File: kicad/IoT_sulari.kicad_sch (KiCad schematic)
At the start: 29 parts, among them J1 73412-0110, J2 73412-0110, J3 20021121-00010C4LF, J4 20021121-00010C4LF, J6 20021121-00010C4LF, SW1 SW_SPST, SW2 TL3301DF160QG, SW3 TL3301DF160QG, SW4 TL3301DF160QG, SW5 TL3301DF160QG, U2 NRF9160-SICA-B1A-R

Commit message: moro
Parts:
- added H1, H2, H3, H4: MountingHole_Pad, MountingHole:MountingHole_3.2mm_M3_Pad_Via, symbol Mechanical:MountingHole_Pad
- U2: value NRF9160-SICA-B1A-R -> NRF9160
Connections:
- net GND: now also J3.3, J3.5, H1.1, H2.1, H3.1, H4.1
- net SWDCLK: now also J3.4; no longer J3.5, J3.6
- net SWDIO: now also J3.2; no longer J3.4, J3.7
- net NRESET: now reaches C10.1, R2.1, U2.32 (NRESET)
- net NRESET: now also J3.10
- no-connect marks 13 -> 15
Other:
- moved on the sheet: D1, D2, R3, R4

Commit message: added board outline and inner copper layers, layout finalization
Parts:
- added R5, R6, R7, R8: 10k, Resistor_SMD:R_0603_1608Metric_Pad0.98x0.95mm_HandSolder, symbol Device:R
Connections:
- net GND: now also R5.1, R6.1, R7.1, R8.1; no longer SW2.3, SW2.4, SW3.3, SW3.4, SW4.3, SW4.4, SW5.3, SW5.4
- new net: R8.2, SW5.3, SW5.4
- new net: R6.2, SW3.3, SW3.4
- new net: R7.2, SW4.3, SW4.4
- new net: R5.2, SW2.3, SW2.4
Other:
- removed sheet sensorboard

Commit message: routing
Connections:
- net BUSY: now also U2.26 (P0-16/AIN3); no longer U2.29 (P0-18/AIN5)
- net CS: now also U2.28 (P0-17/AIN4); no longer U2.25 (P0-15/AIN2)
- net DC: now also U2.25 (P0-15/AIN2); no longer U2.26 (P0-16/AIN3)
- net RST: now also U2.29 (P0-18/AIN5); no longer U2.28 (P0-17/AIN4)
- net SCL: now also U2.86 (P0-28); no longer U2.84 (P0-27)
- net SDA: now also U2.84 (P0-27); no longer U2.83 (P0-26)
- net TMP_ALERT: now also U2.83 (P0-26); no longer U2.86 (P0-28)
- net +3.3V: no longer names the net of C1.1, C2.1, C3.1, FB1.2
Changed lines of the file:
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@@
-    (effects (font (size 1.27 1.27)) (justify left bottom))
-  )
-  (label "+3.3V" (at 101.6 24.13 0) (fields_autoplaced)
     (effects (font (size 1.27 1.27)) (justify left bottom))
   )
@@
     )
   )
-  (global_label "TMP_ALERT" (shape input) (at 222.25 111.76 0) (fields_autoplaced)
+  (global_label "TMP_ALERT" (shape input) (at 222.25 106.68 0) (fields_autoplaced)
     (effects (font (size 1.27 1.27)) (justify left))
-    (property "Intersheetrefs" "${INTERSHEET_REFS}" (at 235.3157 111.76 0)
+    (property "Intersheetrefs" "${INTERSHEET_REFS}" (at 235.3157 106.68 0)
       (effects (font (size 1.27 1.27)) (justify left) hide)
     )
   )
-  (global_label "BUSY" (shape input) (at 152.4 119.38 180) (fields_autoplaced)
-    (effects (font (size 1.27 1.27)) (justify right))
-    (property "Intersheetrefs" "${INTERSHEET_REFS}" (at 144.5956 119.38 0)
+  (global_label "BUSY" (shape input) (at 152.4 114.3 180) (fields_autoplaced)
+    (effects (font (size 1.27 1.27)) (justify right))
+    (property "Intersheetrefs" "${INTERSHEET_REFS}" (at 144.5956 114.3 0)
       (effects (font (size 1.27 1.27)) (justify right) hide)
     )
@@
     )
   )
-  (global_label "RST" (shape input) (at 152.4 116.84 180) (fields_autoplaced)
-    (effects (font (size 1.27 1.27)) (justify right))
-    (property "Intersheetrefs" "${INTERSHEET_REFS}" (at 146.0471 116.84 0)
+  (global_label "RST" (shape input) (at 152.4 119.38 180) (fields_autoplaced)
+    (effects (font (size 1.27 1.27)) (justify right))
+    (property "Intersheetrefs" "${INTERSHEET_REFS}" (at 146.0471 119.38 0)
       (effects (font (size 1.27 1.27)) (justify right) hide)
     )
@@
     )
   )
-  (global_label "CS" (shape input) (at 152.4 111.76 180) (fields_autoplaced)
-    (effects (font (size 1.27 1.27)) (justify right))
-    (property "Intersheetrefs" "${INTERSHEET_REFS}" (at 147.0147 111.76 0)
+  (global_label "CS" (shape input) (at 152.4 116.84 180) (fields_autoplaced)
+    (effects (font (size 1.27 1.27)) (justify right))
+    (property "Intersheetrefs" "${INTERSHEET_REFS}" (at 147.0147 116.84 0)
       (effects (font (size 1.27 1.27)) (justify right) hide)
     )
@@
     )
   )
-  (global_label "SCL" (shape input) (at 222.25 109.22 0) (fields_autoplaced)
+  (global_label "SCL" (shape input) (at 222.25 111.76 0) (fields_autoplaced)
     (effects (font (size 1.27 1.27)) (justify left))
-    (property "Intersheetrefs" "${INTERSHEET_REFS}" (at 228.6634 109.22 0)
+    (property "Intersheetrefs" "${INTERSHEET_REFS}" (at 228.6634 111.76 0)
       (effects (font (size 1.27 1.27)) (justify left) hide)
     )
@@
     )
   )
-  (global_label "DC" (shape input) (at 152.4 114.3 180) (fields_autoplaced)
-    (effects (font (size 1.27 1.27)) (justify right))
-    (property "Intersheetrefs" "${INTERSHEET_REFS}" (at 146.9542 114.3 0)
+  (global_label "DC" (shape input) (at 152.4 111.76 180) (fields_autoplaced)
+    (effects (font (size 1.27 1.27)) (justify right))
+    (property "Intersheetrefs" "${INTERSHEET_REFS}" (at 146.9542 111.76 0)
       (effects (font (size 1.27 1.27)) (justify right) hide)
     )
@@
     )
   )
-  (global_label "SDA" (shape input) (at 222.25 106.68 0) (fields_autoplaced)
+  (global_label "SDA" (shape input) (at 222.25 109.22 0) (fields_autoplaced)
     (effects (font (size 1.27 1.27)) (justify left))
-    (property "Intersheetrefs" "${INTERSHEET_REFS}" (at 228.7239 106.68 0)
+    (property "Intersheetrefs" "${INTERSHEET_REFS}" (at 228.7239 109.22 0)
       (effects (font (size 1.27 1.27)) (justify left) hide)
     )
@@
   (symbol (lib_name "+3.3V_2") (lib_id "power:+3.3V") (at 86.36 21.59 0) (unit 1)
     (in_bom yes) (on_board yes) (dnp no) (fields_autoplaced)
-    (property "Reference" "#PWR011" (at 86.36 25.4 0)
+    (property "Reference" "#PWR0106" (at 86.36 25.4 0)
       (effects (font (size 1.27 1.27)) hide)
     )
@@
       (project "IoT_sulari"
         (path "/184b47ed-2c2b-4c02-be35-d18f4f4e5685"
-          (reference "#PWR011") (unit 1)
+          (reference "#PWR0106") (unit 1)
         )
       )
@@
   (symbol (lib_name "+3.3V_1") (lib_id "power:+3.3V") (at 123.19 31.75 0) (unit 1)
     (in_bom yes) (on_board yes) (dnp no) (fields_autoplaced)
-    (property "Reference" "#PWR012" (at 123.19 35.56 0)
+    (property "Reference" "#PWR0104" (at 123.19 35.56 0)
       (effects (font (size 1.27 1.27)) hide)
     )
@@
       (project "IoT_sulari"
         (path "/184b47ed-2c2b-4c02-be35-d18f4f4e5685"
-          (reference "#PWR012") (unit 1)
+          (reference "#PWR0104") (unit 1)
         )
       )
@@
   (symbol (lib_name "+3.3V_3") (lib_id "power:+3.3V") (at 118.11 48.26 0) (unit 1)
     (in_bom yes) (on_board yes) (dnp no) (fields_autoplaced)
-    (property "Reference" "#PWR025" (at 118.11 52.07 0)
+    (property "Reference" "#PWR0105" (at 118.11 52.07 0)
       (effects (font (size 1.27 1.27)) hide)
     )
@@
       (project "IoT_sulari"
         (path "/184b47ed-2c2b-4c02-be35-d18f4f4e5685"
-          (reference "#PWR025") (unit 1)
-        )
-      )
+          (reference "#PWR0105") (unit 1)
+        )
+      )

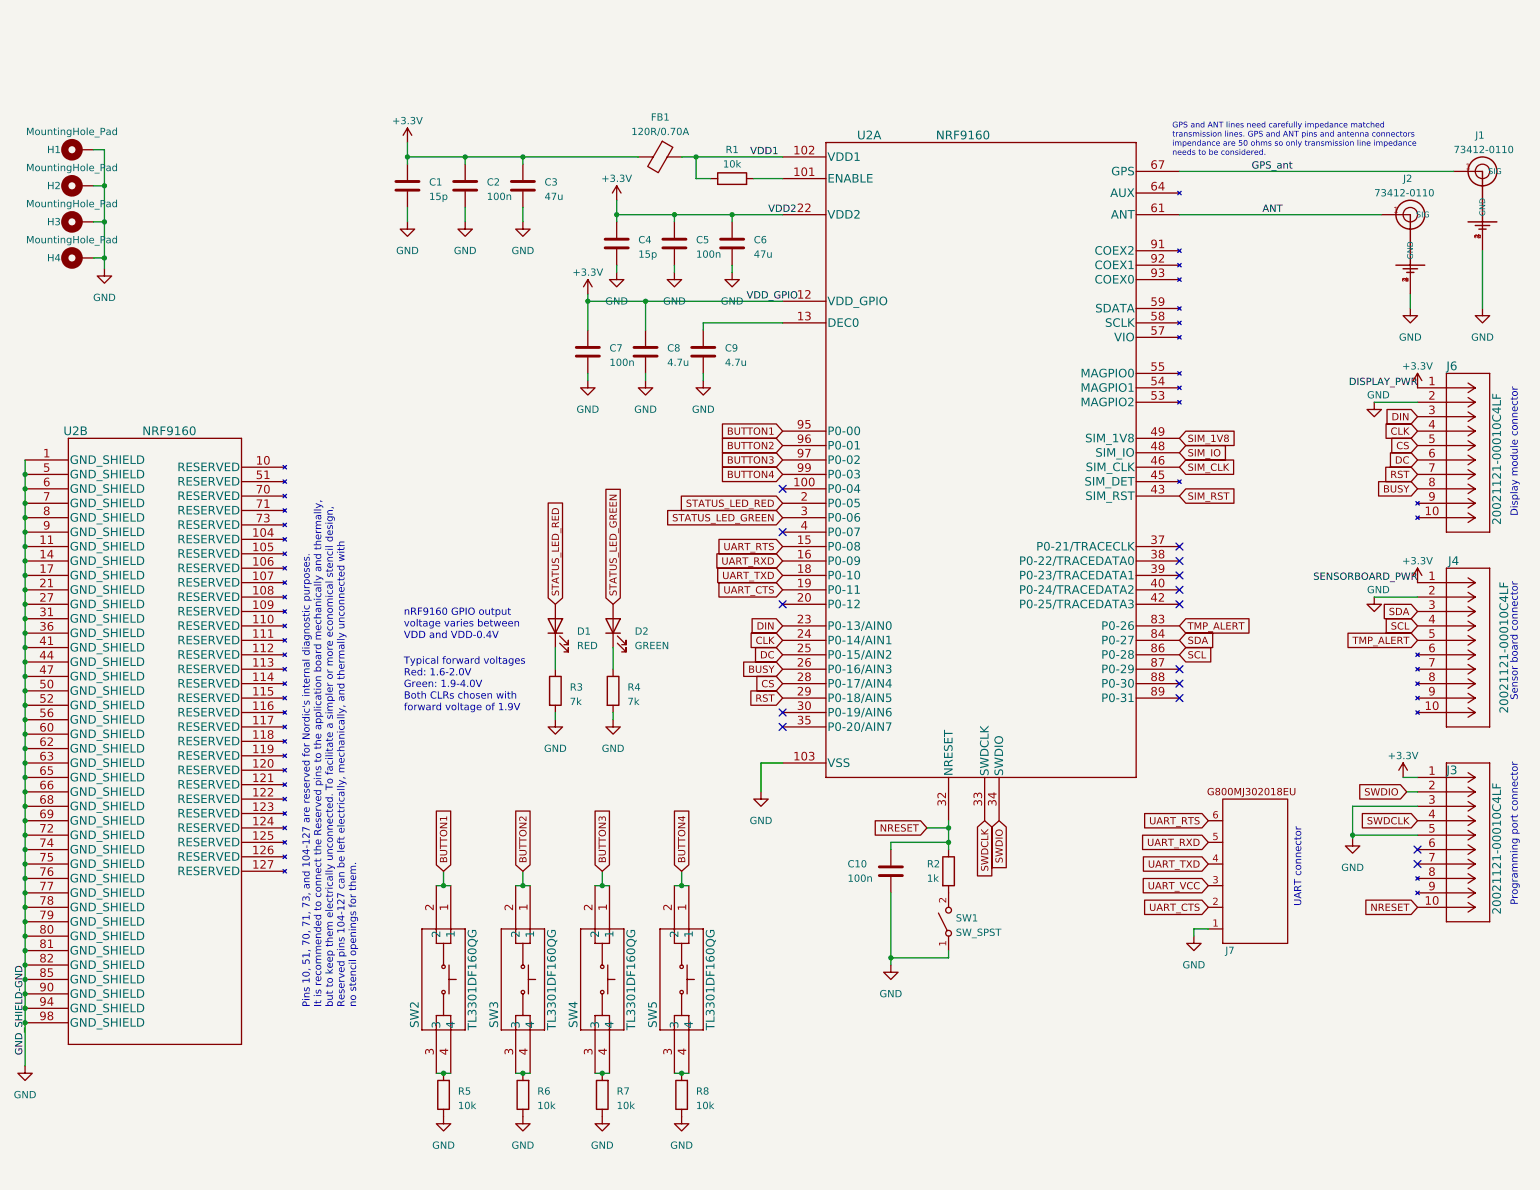
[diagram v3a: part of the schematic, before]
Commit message: Finished routing and added vias
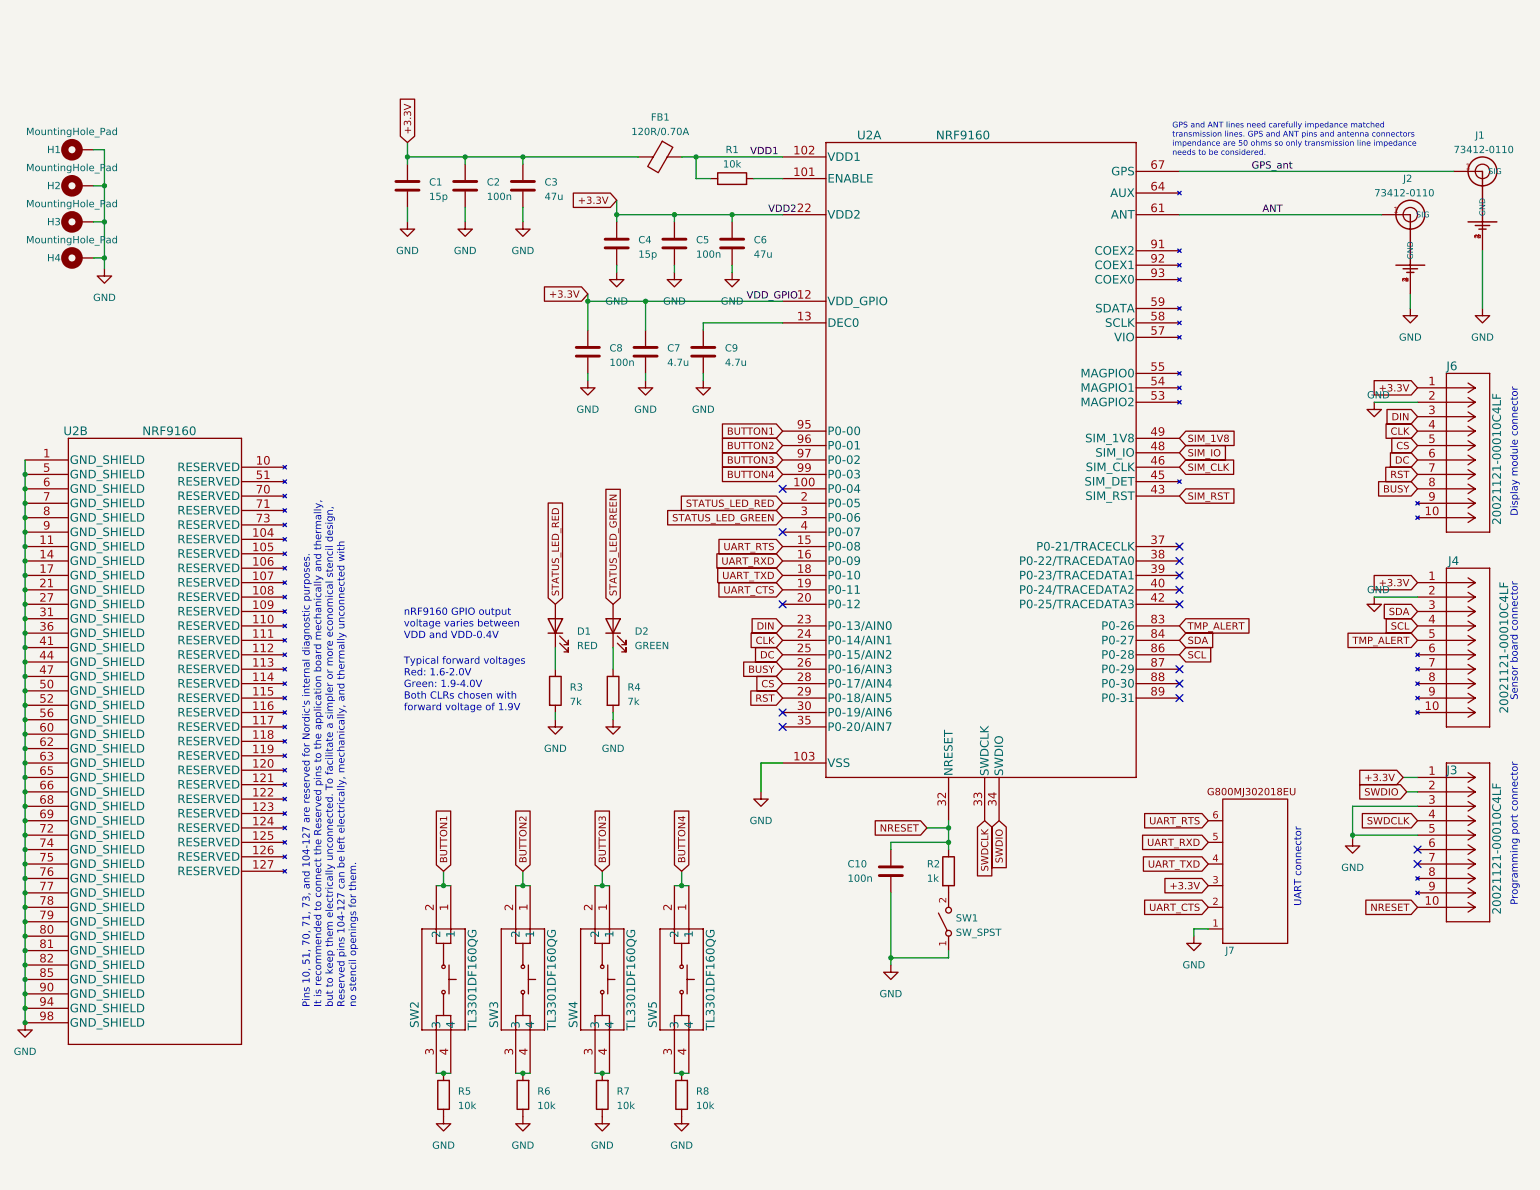
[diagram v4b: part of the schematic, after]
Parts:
- renumbered C8 to C7, C7 to C8
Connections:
- net DISPLAY_PWR is gone; now on net +3.3V: J6.1
- net GND_SHIELD-GND is gone; now on net GND: U2.1 (GND_SHIELD), U2.11 (GND_SHIELD), U2.14 (GND_SHIELD), U2.17 (GND_SHIELD), U2.21 (GND_SHIELD), U2.27 (GND_SHIELD), U2.31 (GND_SHIELD), U2.36 (GND_SHIELD), U2.41 (GND_SHIELD), U2.44 (GND_SHIELD), U2.47 (GND_SHIELD), U2.5 (GND_SHIELD), U2.50 (GND_SHIELD), U2.52 (GND_SHIELD), U2.56 (GND_SHIELD), U2.6 (GND_SHIELD), U2.60 (GND_SHIELD), U2.62 (GND_SHIELD), U2.63 (GND_SHIELD), U2.65 (GND_SHIELD), U2.66 (GND_SHIELD), U2.68 (GND_SHIELD), U2.69 (GND_SHIELD), U2.7 (GND_SHIELD), U2.72 (GND_SHIELD), U2.74 (GND_SHIELD), U2.75 (GND_SHIELD), U2.76 (GND_SHIELD), U2.77 (GND_SHIELD), U2.78 (GND_SHIELD), U2.79 (GND_SHIELD), U2.8 (GND_SHIELD), U2.80 (GND_SHIELD), U2.81 (GND_SHIELD), U2.82 (GND_SHIELD), U2.85 (GND_SHIELD), U2.9 (GND_SHIELD), U2.90 (GND_SHIELD), U2.94 (GND_SHIELD), U2.98 (GND_SHIELD)
- net SENSORBOARD_PWR is gone; now on net +3.3V: J4.1
- net UART_VCC is gone; now on net +3.3V: J7.3
- net VDD2 is gone; now on net +3.3V: C4.1, C5.1, C6.1, U2.22 (VDD2)
- net VDD_GPIO is gone; now on net +3.3V: C7.1, C8.1, U2.12 (VDD_GPIO)
- net +3.3V: now reaches C1.1, C2.1, C3.1, FB1.2
- net +3.3V: now also J3.1
